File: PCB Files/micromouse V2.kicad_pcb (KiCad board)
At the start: 2 copper layers, 100 x 130 mm, 50 parts, among them J1 USB-C, J10 TOF1, J11 Motor 1, J12 TOF1, J13 Motor 2, J14 TOF1, J7 BATT, J8 TOF1, J9 TOF1, SW1 SW_Push, SW2 SW_Push, SW3 SW_Push, U1 STM32F103C8Tx, U3 AMS1117-3.3, U4 SSD1306, U5 L7805, U6 L7806, U8 TB6612FNG, Y1 Crystal

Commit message: Fixed PCB Layout
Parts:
- removed the D1 at (244.2, 85.9)
- removed J10, J12, J14: TOF1, Connector_PinSocket_2.54mm:PinSocket_1x06_P2.54mm_Vertical
- removed the J8 at (195.9, 96.2)
- added C15: 0.1uF, Capacitor_SMD:C_0805_2012Metric_Pad1.18x1.45mm_HandSolder, F.Cu at (143.1, 150.0)
- added C16: 0.1uF, Capacitor_SMD:C_0805_2012Metric_Pad1.18x1.45mm_HandSolder, F.Cu at (143.1, 156.2)
- added C17: 0.1uF, Capacitor_SMD:C_0805_2012Metric_Pad1.18x1.45mm_HandSolder, F.Cu at (143.1, 162.4)
- added C18: 1uF, Capacitor_SMD:C_0805_2012Metric_Pad1.18x1.45mm_HandSolder, F.Cu at (70.2, 89.4)
- added C22: 20p, Capacitor_SMD:C_0805_2012Metric_Pad1.18x1.45mm_HandSolder, F.Cu at (128.0, 74.8)
- added D5: USB, LED_SMD:LED_0805_2012Metric_Pad1.15x1.40mm_HandSolder, F.Cu at (69.2, 147.5)
- added D6: SP0503BAHT, Package_TO_SOT_SMD:SOT-143, F.Cu at (75.3, 159.0)
- added J2: TOF1, Connector_PinSocket_2.54mm:PinSocket_1x06_P2.54mm_Vertical, F.Cu at (104.7, 45.5)
- added J3: Conn_02x02_Counter_Clockwise, Connector_PinHeader_2.54mm:PinHeader_2x02_P2.54mm_Vertical, F.Cu at (109.7, 100.0)
- added J5: TOF1, Connector_PinSocket_2.54mm:PinSocket_1x06_P2.54mm_Vertical, F.Cu at (157.5, 73.9)
- added J6: Conn_01x02_Pin, Connector_PinHeader_2.54mm:PinHeader_1x02_P2.54mm_Vertical, F.Cu at (157.8, 96.0)
- added R10: 220R, Resistor_SMD:R_0805_2012Metric_Pad1.20x1.40mm_HandSolder, F.Cu at (64.4, 147.5)
- added R3: 47R, Resistor_SMD:R_0805_2012Metric_Pad1.20x1.40mm_HandSolder, F.Cu at (105.2, 147.9)
- added R5: 1M, Resistor_SMD:R_0805_2012Metric_Pad1.20x1.40mm_HandSolder, F.Cu at (133.0, 65.0)
- added R6: 47R, Resistor_SMD:R_0805_2012Metric_Pad1.20x1.40mm_HandSolder, F.Cu at (119.5, 78.5)
- added R7: 10K, Resistor_SMD:R_0805_2012Metric_Pad1.20x1.40mm_HandSolder, F.Cu at (143.1, 147.0)
- added R8: 10K, Resistor_SMD:R_0805_2012Metric_Pad1.20x1.40mm_HandSolder, F.Cu at (143.1, 153.1)
- added R9: 10K, Resistor_SMD:R_0805_2012Metric_Pad1.20x1.40mm_HandSolder, F.Cu at (143.1, 159.3)
- added SW4: A, Button_Switch_THT:SW_PUSH_6mm_H13mm, F.Cu at (150.2, 145.1)
- added SW5: B, Button_Switch_THT:SW_PUSH_6mm_H13mm, F.Cu at (150.2, 153.7)
- added SW6: C, Button_Switch_THT:SW_PUSH_6mm_H13mm, F.Cu at (150.2, 162.2)
- added SW7: RESET, Button_Switch_THT:SW_PUSH_6mm_H13mm, F.Cu at (64.8, 94.8)
- added Y2: 32.768K, Custom:XTAL_ABS07-32.768KHZ-T, F.Cu at (128.0, 78.2)
- C1: renamed from C17; value 10u -> 10uF
- C19: renamed from C4; value 10p -> 20p
- C2: renamed from C16; value 100n -> 100nF
- C20: renamed from C22; value 10p -> 20p
- C21: value 100n -> 20p
- C3: renamed from C15; value 100n -> 100nF
- C4: renamed from C14; value 100n -> 100nF
- C5: renamed from C13; value 100n -> 100nF
- C6: renamed from C18; value 10n -> 10nF
- C7: renamed from C19; value 1u -> 1uF
- C8: renamed from C20; value 1u -> 1uF
- FB1: footprint Resistor_SMD:R_0805_2012Metric_Pad1.20x1.40mm_HandSolder -> Inductor_SMD:L_0805_2012Metric
- J1: value USB-C -> TOF1; footprint Connector_USB:USB_C_Receptacle_HRO_TYPE-C-31-M-12 -> Connector_PinSocket_2.54mm:PinSocket_1x06_P2.54mm_Vertical
- J9: value TOF1 -> USB-C; footprint Connector_PinSocket_2.54mm:PinSocket_1x06_P2.54mm_Vertical -> Connector_USB:USB_C_Receptacle_HRO_TYPE-C-31-M-12
- R1: renamed from R5; value 110R -> 330R
- SW1: value SW_Push -> BOOT0; footprint Button_Switch_THT:SW_PUSH_6mm_H13mm -> Button_Switch_THT:SW_Slide_SPDT_Straight_CK_OS102011MS2Q
- SW2: value SW_Push -> BOOT1; footprint Button_Switch_THT:SW_PUSH_6mm_H13mm -> Button_Switch_THT:SW_Slide_SPDT_Straight_CK_OS102011MS2Q
- SW3: value SW_Push -> POWER; footprint Button_Switch_THT:SW_PUSH_6mm_H13mm -> Button_Switch_THT:SW_Slide_SPDT_Straight_CK_OS102011MS2Q
- Y1: value Crystal -> 8MHz; footprint Crystal:Crystal_HC49-4H_Vertical -> Custom:Crystal_ABLS2-8.000MHZ-D4Y-T
- moved J1 191.9 mm to (64.5, 73.9)
- moved C12 175.3 mm to (87.4, 153.5), turned to 90 degrees
- moved C11 168.6 mm to (82.3, 153.5), turned to 90 degrees
- moved U1 165.0 mm to (85.9, 164.7), turned to 90 degrees
- moved C13 163.7 mm to (92.5, 153.5), turned to 90 degrees
- moved J7 160.4 mm to (81.2, 96.5)
- moved U3 160.2 mm to (93.6, 164.7), turned to 90 degrees
- moved C9 158.1 mm to (102.7, 153.5), turned to 90 degrees
- moved C14 156.3 mm to (97.6, 153.5), turned to 90 degrees
- moved SW3 153.3 mm to (72.4, 167.4), turned to 180 degrees
- moved C10 152.2 mm to (107.8, 153.5), turned to 90 degrees
- moved R4 151.8 mm to (70.2, 86.7)
- moved SW2 151.5 mm to (88.8, 76.1)
- moved SW1 150.2 mm to (88.8, 70.5)
- moved J9 148.0 mm to (65.1, 156.0), turned to -90 degrees
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- renumbered C2 to C10, C8 to C11, C11 to C12, C3 to C13, C5 to C14, C1 to C9, D2 to D1, D5 to D2, D6 to D4, J7 to J4, J11 to J7, J13 to J8, R1 to R11, R4 to R2, R3 to R4, U6 to U1, U3 to U2, U5 to U3, U1 to U4, U4 to U5, U8 to U6
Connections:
- C11 pad 2: +7.4V -> POWER
- C13 pad 1: +7.4V -> POWER
- C19 pad 2: GND -> Net-(C19-Pad2)
- C20 pad 2: GND -> Net-(C19-Pad2)
- C21 pad 1: /NRST -> OSC32_IN
- C9 pad 1: +7.4V -> POWER
- D1 pad 2: +3.3V -> Net-(D1-A)
- D4 pad 1: PC13 -> Net-(D4-K)
- R4 pad 1: BOOT0 -> +3.3V
- R4 pad 2: Net-(SW4-B) -> RESET
- SW1 pad 2: SW1 -> BOOT0
- SW2 pad 2: SW2 -> BOOT1
- SW3 pad 1: GND -> +7.4V
- SW3 pad 2: SW3 -> POWER
- U1 pad 1: +7.4V -> POWER
- U2 pad 3: +7.4V -> POWER
- U3 pad 1: +7.4V -> POWER
- U4 pad 20: unconnected-(U1-PB2-Pad20) -> BOOT1
- U4 pad 3: unconnected-(U1-PC14-Pad3) -> OSC32_IN
- U4 pad 34: unconnected-(U1-PA13-Pad34) -> SWDIO
- U4 pad 37: unconnected-(U1-PA14-Pad37) -> SWCLK
- U4 pad 4: unconnected-(U1-PC15-Pad4) -> OSC32_OUT
- U4 pad 7: /NRST -> RESET
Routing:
- net GND: track 0.00 -> 556.3 mm, vias 0 -> 10
- net +3.3V: track 0.00 -> 467.7 mm, vias 0 -> 11
- net +5V: track 0.00 -> 177.0 mm, vias 0 -> 5
- net SDA1: track 0.00 -> 169.1 mm, vias 0 -> 5
- net SCL1: track 0.00 -> 150.2 mm, vias 0 -> 1
- net SW3: track 0.00 -> 144.0 mm, vias 0 -> 3
- net SW2: track 0.00 -> 139.0 mm, vias 0 -> 3
- net SW1: track 0.00 -> 128.6 mm, vias 0 -> 3
- net USB_D+: track 0.00 -> 124.7 mm
- net SCL2: track 0.00 -> 123.9 mm, vias 0 -> 3
- net SDA2: track 0.00 -> 120.8 mm, vias 0 -> 3
- net USB_D-: track 0.00 -> 115.0 mm, vias 0 -> 2
- net +6V: track 0.00 -> 107.4 mm, vias 0 -> 2
- net RESET: track 0.00 -> 70.0 mm, vias 0 -> 1
- net PA7: track 0.00 -> 68.4 mm, vias 0 -> 2
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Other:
- outline, holes or cut-outs redrawn
- board text added: "0"
- board text added: "1"
- board text added: "3V3"
- board text added: "GND"
- board text added: "MICROMOUSE V2"
- board text added: "OFF"
- board text added: "ON"
- board text added: "SWCLK"
- board text added: "SWDIO"
- board text removed: "MICROMOUSE V1"

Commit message: default
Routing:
- net GND: track 556.3 -> 149.3 mm, vias 10 -> 4
- net PA3: track 0.00 -> 41.2 mm, vias 0 -> 2
- net +3.3V: track 467.7 -> 443.3 mm
- net PA4: track 0.00 -> 24.0 mm, vias 0 -> 2
- net POWER: track 61.1 -> 82.8 mm
- net +6V: track 107.4 -> 119.3 mm, vias 2 -> 4
- net HSE_IN: track 19.1 -> 23.5 mm
- net SCL1: track 150.2 -> 154.5 mm
- net BOOT0: track 36.6 -> 38.7 mm
- net SDA2: track 120.8 -> 122.1 mm
- net SCL2: track 123.9 -> 124.9 mm
- net TXD: track 61.5 -> 62.2 mm
- net PA5: track 28.1 -> 27.6 mm
- added copper zone on B.Cu, net GND
- added copper zone on F.Cu, net GND

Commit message: default
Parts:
- added C23: 10nF, Capacitor_SMD:C_0805_2012Metric, F.Cu at (118.9, 113.1)
- added C24: 100nF, Capacitor_SMD:C_0805_2012Metric, F.Cu at (103.7, 108.1)
- added C25: 100nF, Capacitor_SMD:C_0805_2012Metric, F.Cu at (118.9, 107.5)
- added C26: 2.2nF, Capacitor_SMD:C_0805_2012Metric, F.Cu at (118.9, 104.7)
- added D7: GYRO, LED_SMD:LED_0805_2012Metric, F.Cu at (121.3, 99.0)
- added R12: 4.7K, Resistor_SMD:R_0805_2012Metric, F.Cu at (103.7, 113.3)
- added R13: 4.7K, Resistor_SMD:R_0805_2012Metric, F.Cu at (103.7, 110.4)
- added R14: 4.7K, Resistor_SMD:R_0805_2012Metric, F.Cu at (118.9, 110.3)
- added R15: 47R, Resistor_SMD:R_0805_2012Metric, F.Cu at (103.7, 105.8)
- added U7: MPU-6050, Sensor_Motion:InvenSense_QFN-24_4x4mm_P0.5mm, F.Cu at (111.0, 110.1)
- C1, C10, C11, C12, C13, C14, C18, C19, C2, C20, C21, C22, C3, C4, C5, C6, C7, C8, C9: footprint Capacitor_SMD:C_0805_2012Metric_Pad1.18x1.45mm_HandSolder -> Capacitor_SMD:C_0805_2012Metric
- C15, C16, C17: value 0.1uF -> 100nF; footprint Capacitor_SMD:C_0805_2012Metric_Pad1.18x1.45mm_HandSolder -> Capacitor_SMD:C_0805_2012Metric
- D1, D2, D3, D4, D5: footprint LED_SMD:LED_0805_2012Metric_Pad1.15x1.40mm_HandSolder -> LED_SMD:LED_0805_2012Metric
- R1, R10, R11, R2, R3, R4, R5, R6, R7, R8, R9: footprint Resistor_SMD:R_0805_2012Metric_Pad1.20x1.40mm_HandSolder -> Resistor_SMD:R_0805_2012Metric
- SW1, SW2, SW3: footprint Button_Switch_THT:SW_Slide_SPDT_Straight_CK_OS102011MS2Q -> Custom:SW_SS12D07VG4
- moved SW1 2.11 mm to (90.8, 70.0)
- moved SW2 2.11 mm to (90.8, 75.6)
- moved SW3 1.80 mm to (70.6, 167.4)
- moved R7 0.06 mm to (143.1, 146.9)
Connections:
- net OSC32_IN renamed LSE_IN
- net OSC32_OUT renamed LSE_OUT
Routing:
- net +3.3V: track 443.3 -> 472.6 mm
- net SDA2: track 122.1 -> 147.7 mm, vias 3 -> 4
- net Net-(D7-A): track 0.00 -> 19.7 mm
- net SCL2: track 124.9 -> 144.1 mm, vias 3 -> 4
- net Net-(U7-REGOUT): track 0.00 -> 11.5 mm
- net Net-(U7-AD0): track 0.00 -> 9.98 mm
- net Net-(U7-CPOUT): track 0.00 -> 7.90 mm
- net SW3: track 144.0 -> 151.5 mm
- net PA3: track 41.2 -> 42.9 mm
- net BOOT0: track 38.7 -> 40.2 mm
- net GND: track 149.3 -> 150.3 mm, vias 4 -> 5
- net +6V: track 119.3 -> 119.2 mm, vias 4 -> 3

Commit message: Fixed
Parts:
- moved R15 0.78 mm to (103.7, 105.0)
- moved C24 0.39 mm to (103.7, 107.7)
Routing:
- net SCL2: track 144.1 -> 145.8 mm
- net GND: track 150.3 -> 151.9 mm
- net OUT1: track 20.6 -> 21.3 mm

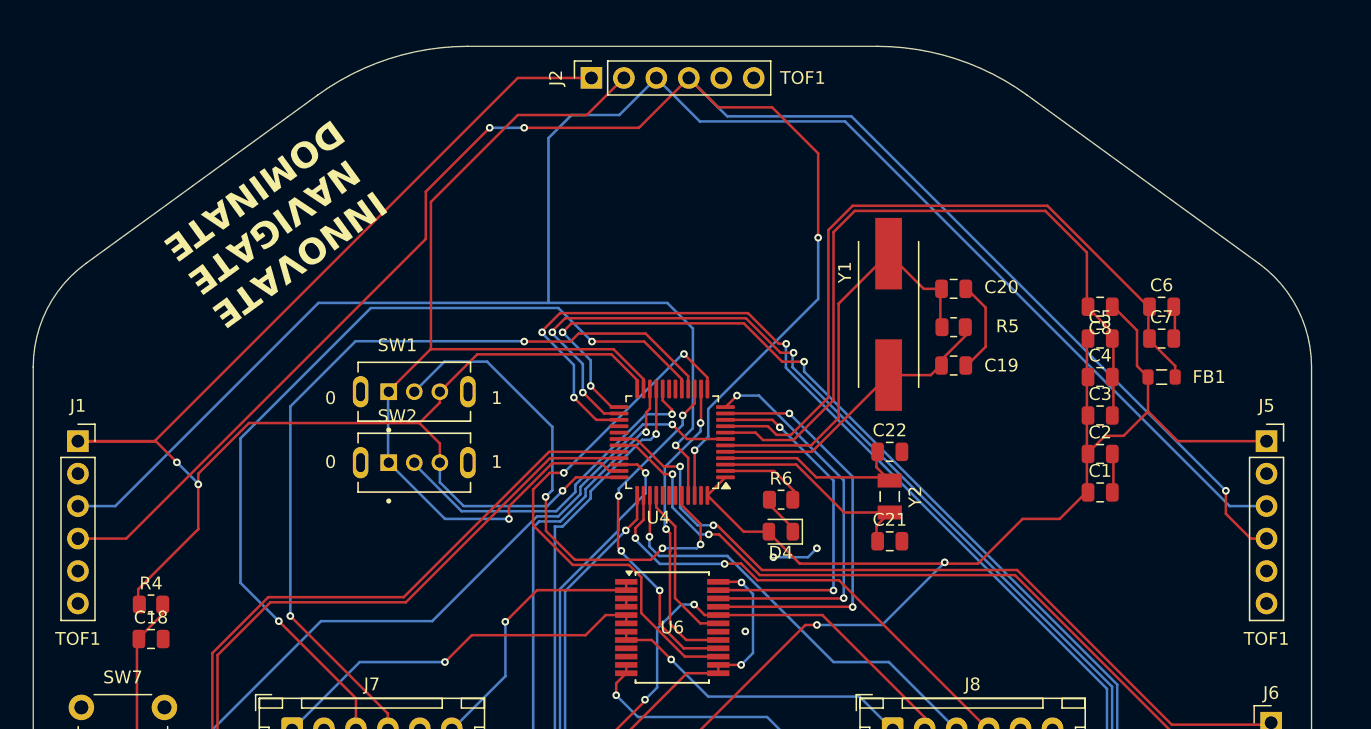
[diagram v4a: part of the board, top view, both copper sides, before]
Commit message: Flipped TOF
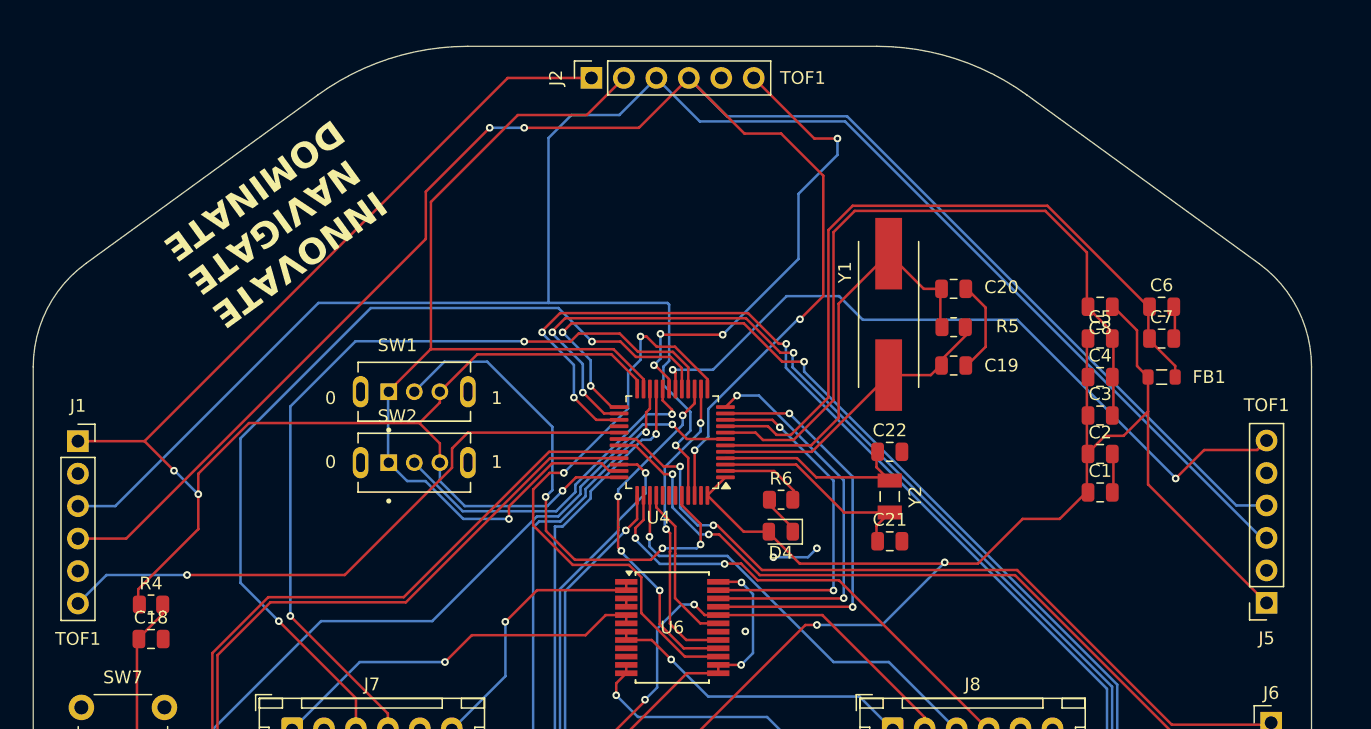
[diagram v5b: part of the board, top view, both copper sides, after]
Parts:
- moved J5 12.6 mm to (157.5, 86.6), turned to 180 degrees
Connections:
- J1 pad 6: unconnected-(J1-Pin_6-Pad6) -> XSHUT1
- J2 pad 6: unconnected-(J2-Pin_6-Pad6) -> XSHUT2
- J5 pad 6: unconnected-(J5-Pin_6-Pad6) -> XSHUT3
- U4 pad 18: unconnected-(U4-PB0-Pad18) -> XSHUT3
- U4 pad 19: unconnected-(U4-PB1-Pad19) -> XSHUT2
- U4 pad 29: unconnected-(U4-PA8-Pad29) -> XSHUT1
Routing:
- net XSHUT3: track 0.00 -> 57.6 mm, vias 0 -> 2
- net XSHUT1: track 0.00 -> 48.8 mm, vias 0 -> 1
- net XSHUT2: track 0.00 -> 37.6 mm, vias 0 -> 4
- net PA3: track 42.9 -> 46.7 mm
- net +3.3V: track 472.7 -> 476.3 mm
- net SDA1: track 169.4 -> 166.9 mm, vias 5 -> 4
- net SCL1: track 154.5 -> 155.7 mm
- net PA7: track 68.4 -> 68.9 mm
